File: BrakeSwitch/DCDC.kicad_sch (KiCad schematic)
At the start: 7 parts, among them U1 XL1509-5.0

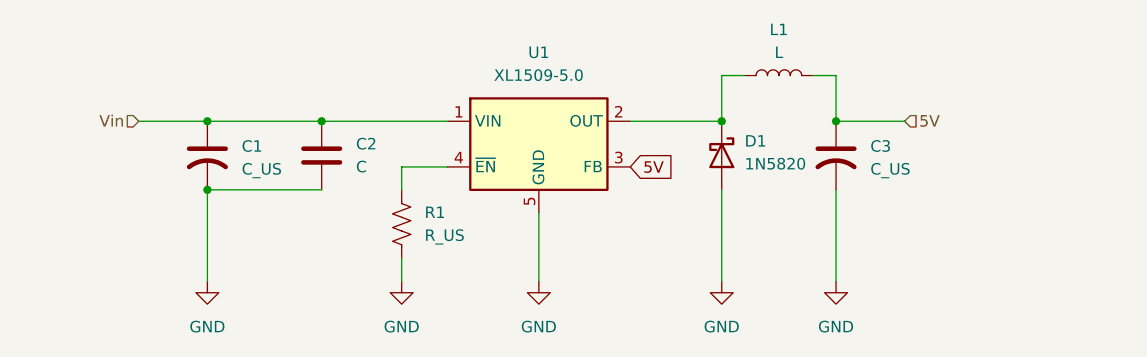
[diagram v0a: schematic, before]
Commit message: Assigned most footprints
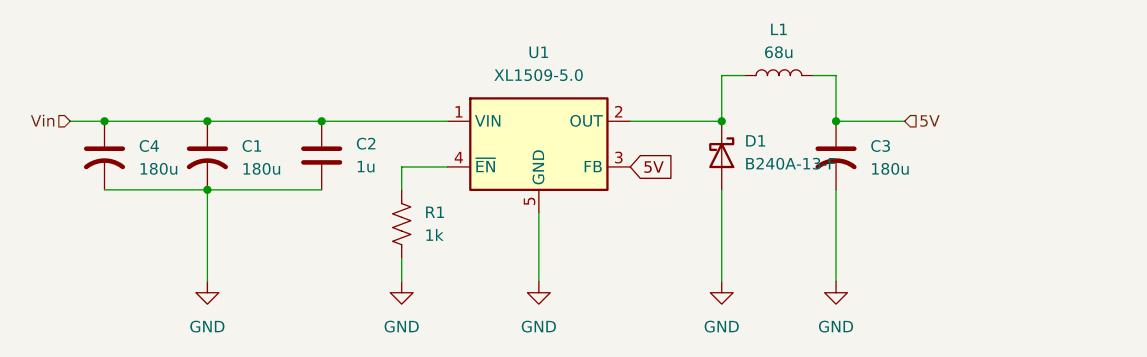
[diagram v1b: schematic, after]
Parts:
- added C4: 180u, Capacitor_SMD:CP_Elec_8x10.5, symbol Device:C_US
- C1, C3: value C_US -> 180u; footprint (none) -> Capacitor_SMD:CP_Elec_8x10.5
- C2: value C -> 1u; footprint (none) -> Capacitor_SMD:C_0603_1608Metric_Pad1.08x0.95mm_HandSolder
- D1: value 1N5820 -> B240A-13-F; footprint (none) -> Diode_SMD:D_SMA; DigiKey (none) -> https://www.digikey.com/en/products/detail/diodes-incorpora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
- L1: value L -> 68u; footprint (none) -> Inductor_SMD:L_12x12mm_H4.5mm; DigiKey (none) -> https://www.digikey.com/en/products/detail/sumida-america-i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
- R1: value R_US -> 1k; footprint (none) -> Resistor_SMD:R_0603_1608Metric
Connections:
- net GND: now also C4.2
- net Vin: now also C4.1
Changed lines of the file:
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@@
+	)
+	(junction
+		(at 20.32 26.67)
+		(diameter 0)
+		(color 0 0 0 0)
+	)
+	(junction
+		(at 31.75 34.29)
+		(diameter 0)
+		(color 0 0 0 0)
 	)
 	(junction
@@
 		(color 0 0 0 0)
 	)
-	(junction
-		(at 31.75 34.29)
-		(diameter 0)
-		(color 0 0 0 0)
-	)
 	(wire
 		(pts
@@
 	(wire
 		(pts
-			(xy 24.13 26.67) (xy 31.75 26.67)
+			(xy 31.75 26.67) (xy 44.45 26.67)
 		)
 		(stroke
@@
 	(wire
 		(pts
-			(xy 88.9 21.59) (xy 91.44 21.59)
+			(xy 16.51 26.67) (xy 20.32 26.67)
 		)
 		(stroke
@@
 	(wire
 		(pts
-			(xy 101.6 34.29) (xy 101.6 44.45)
+			(xy 88.9 21.59) (xy 91.44 21.59)
 		)
 		(stroke
@@
 	(wire
 		(pts
-			(xy 68.58 36.83) (xy 68.58 44.45)
+			(xy 20.32 26.67) (xy 31.75 26.67)
 		)
 		(stroke
@@
 	(wire
 		(pts
-			(xy 31.75 26.67) (xy 44.45 26.67)
+			(xy 101.6 34.29) (xy 101.6 44.45)
 		)
 		(stroke
@@
 	(wire
 		(pts
-			(xy 88.9 34.29) (xy 88.9 44.45)
+			(xy 68.58 36.83) (xy 68.58 44.45)
 		)
 		(stroke
@@
 	(wire
 		(pts
-			(xy 101.6 21.59) (xy 101.6 26.67)
+			(xy 88.9 34.29) (xy 88.9 44.45)
 		)
 		(stroke
@@
 	(wire
 		(pts
-			(xy 101.6 26.67) (xy 109.22 26.67)
+			(xy 101.6 21.59) (xy 101.6 26.67)
 		)
 		(stroke
@@
 	(wire
 		(pts
-			(xy 78.74 26.67) (xy 88.9 26.67)
+			(xy 101.6 26.67) (xy 109.22 26.67)
 		)
 		(stroke
@@
 	(wire
 		(pts
+			(xy 78.74 26.67) (xy 88.9 26.67)
+		)
+		(stroke
+			(width 0)
+			(type default)
+		)
+	)
+	(wire
+		(pts
 			(xy 53.34 34.29) (xy 53.34 31.75)
+		)
+		(stroke
+			(width 0)
+			(type default)
+		)
+	)
+	(wire
+		(pts
+			(xy 31.75 34.29) (xy 20.32 34.29)
 		)
 		(stroke
@@
 	(hierarchical_label "Vin"
 		(shape input)
-		(at 24.13 26.67 180)
+		(at 16.51 26.67 180)
 		(effects
 			(font
@@
 	(symbol
 		(lib_id "Device:C_US")
+		(at 20.32 30.48 0)
+		(unit 1)
+		(exclude_from_sim no)
+		(in_bom yes)
+		(on_board yes)
+		(dnp no)
+		(fields_autoplaced yes)
+		(property "Reference" "C4"
+			(at 24.13 29.4639 0)
+			(effects
+				(font
+					(size 1.27 1.27)
+				)
+				(justify left)
+			)
+		)
+		(property "Value" "180u"
+			(at 24.13 32.0039 0)
+			(effects
+				(font
+					(size 1.27 1.27)
+				)
+				(justify left)
+			)
+		)
+		(property "Footprint" "Capacitor_SMD:CP_Elec_8x10.5"
+			(at 20.32 30.48 0)
+			(effects
+				(font
+					(size 1.27 1.27)
+				)
+				(hide yes)
+			)
+		)
+		(property "Datasheet" ""
+			(at 20.32 30.48 0)
+			(effects
+				(font
+					(size 1.27 1.27)
+				)
+				(hide yes)
+			)
+		)
+		(property "Description" "capacitor, US symbol"
+			(at 20.32 30.48 0)
+			(effects
+				(font
+					(size 1.27 1.27)
+				)
+				(hide yes)
+			)
+		)
+		(pin "2"
+		)
+		(pin "1"
+		)
+		(instances
+			(project "BrakeSwitch"
+				(path "/fe3f2fb8-8742-4f31-813f-1dad9d418d71/293b1cf4-e9c5-4398-be38-45432f0835da"
+					(reference "C4")
+					(unit 1)
+				)
+			)
+		)
+	)
+	(symbol
+		(lib_id "Device:C_US")
 		(at 101.6 30.48 0)
 		(unit 1)
@@
 			)
 		)
-		(property "Value" "C_US"
+		(property "Value" "180u"
 			(at 105.41 32.0039 0)
 			(effects
@@
 			)
 		)
-		(property "Footprint" ""
+		(property "Footprint" "Capacitor_SMD:CP_Elec_8x10.5"
 			(at 101.6 30.48 0)
 			(effects
@@
 			)
 		)
-		(property "Value" "R_US"
+		(property "Value" "1k"
 			(at 55.88 39.3699 0)
 			(effects
@@
 			)
 		)
-		(property "Footprint" ""
+		(property "Footprint" "Resistor_SMD:R_0603_1608Metric"
 			(at 54.356 38.354 90)
 			(effects
@@
 				(path "/fe3f2fb8-8742-4f31-813f-1dad9d418d71/293b1cf4-e9c5-4398-be38-45432f0835da"
 					(reference "R1")
+					(unit 1)
+				)
+			)
+		)
+	)
+	(symbol
+		(lib_id "Device:C_US")
+		(at 31.75 30.48 0)
+		(unit 1)
+		(exclude_from_sim no)
+		(in_bom yes)
+		(on_board yes)
+		(dnp no)
+		(fields_autoplaced yes)
+		(property "Reference" "C1"
+			(at 35.56 29.4639 0)
+			(effects
+				(font
+					(size 1.27 1.27)
+				)
+				(justify left)
+			)
+		)
+		(property "Value" "180u"
+			(at 35.56 32.0039 0)
+			(effects
+				(font
+					(size 1.27 1.27)
+				)
+				(justify left)
+			)
+		)
+		(property "Footprint" "Capacitor_SMD:CP_Elec_8x10.5"
+			(at 31.75 30.48 0)
+			(effects
+				(font
+					(size 1.27 1.27)
+				)
+				(hide yes)
+			)
+		)
+		(property "Datasheet" ""
+			(at 31.75 30.48 0)
+			(effects
+				(font
+					(size 1.27 1.27)
+				)
+				(hide yes)
+			)
+		)
+		(property "Description" "capacitor, US symbol"
+			(at 31.75 30.48 0)
+			(effects
+				(font
+					(size 1.27 1.27)
+				)
+				(hide yes)
+			)
+		)
+		(pin "2"
+		)
+		(pin "1"
+		)
+		(instances
+			(project "BrakeSwitch"
+				(path "/fe3f2fb8-8742-4f31-813f-1dad9d418d71/293b1cf4-e9c5-4398-be38-45432f0835da"
+					(reference "C1")
 					(unit 1)
 				)
@@
 			)
 		)
-		(property "Value" "C"
+		(property "Value" "1u"
 			(at 48.26 31.7499 0)
 			(effects
@@
 			)
 		)
-		(property "Footprint" ""
+		(property "Footprint" "Capacitor_SMD:C_0603_1608Metric_Pad1.08x0.95mm_HandSolder"
 			(at 45.4152 34.29 0)
 			(effects
@@
 			)
 		)
-		(property "Value" "1N5820"
+		(property "Value" "B240A-13-F"
 			(at 91.44 31.4324 90)
 			(effects
@@
 			)
 		)
-		(property "Footprint" ""
+		(property "Footprint" "Diode_SMD:D_SMA"
 			(at 88.9 30.48 0)
 			(effects
@@
 			)
 		)
-		(property "Datasheet" "~"
+		(property "Datasheet" "https://www.diodes.com/assets/Datasheets/B220_A-B260_A.pdf"
 			(at 88.9 30.48 0)
 			(effects
@@
 		(property "Description" "Schottky diode"
 			(at 88.9 30.48 0)
+			(effects
+				(font
+					(size 1.27 1.27)
+				)
+				(hide yes)
+			)
+		)
+		(property "DigiKey" "https://www.digikey.com/en/products/detail/diodes-incorporated/B240A-13-F/717691"
+			(at 88.9 30.48 90)
 			(effects
 				(font
@@
 			)
 		)
-		(property "Value" "L"
+		(property "Value" "68u"
 			(at 95.25 19.05 90)
 			(effects
@@
 			)
 		)
-		(property "Footprint" ""
+		(property "Footprint" "Inductor_SMD:L_12x12mm_H4.5mm"
 			(at 95.25 21.59 0)
 			(effects
@@
 		(property "Description" "Inductor"
 			(at 95.25 21.59 0)
+			(effects
+				(font
+					(size 1.27 1.27)
+				)
+				(hide yes)
+			)
+		)
+		(property "DigiKey" "https://www.digikey.com/en/products/detail/sumida-america-inc/CDRH124NP-680MC/3947049"
+			(at 95.25 21.59 90)
 			(effects
 				(font
@@
 					(unit 1)
 				)
-			)
-		)
-	)
-	(symbol
-		(lib_id "Device:C_US")
-		(at 31.75 30.48 0)
-		(unit 1)
-		(exclude_from_sim no)
-		(in_bom yes)
-		(on_board yes)
-		(dnp no)
-		(fields_autoplaced yes)
-		(property "Reference" "C1"
-			(at 35.56 29.4639 0)
-			(effects
-				(font
-					(size 1.27 1.27)
-				)
-				(justify left)
-			)
-		)
-		(property "Value" "C_US"
-			(at 35.56 32.0039 0)
-			(effects
-				(font
-					(size 1.27 1.27)
-				)
-				(justify left)
-			)
-		)
-		(property "Footprint" ""
-			(at 31.75 30.48 0)
-			(effects
-				(font
-					(size 1.27 1.27)
-				)
-				(hide yes)
-			)
-		)
-		(property "Datasheet" ""
-			(at 31.75 30.48 0)
-			(effects
-				(font
-					(size 1.27 1.27)
-				)
-				(hide yes)
-			)
-		)
-		(property "Description" "capacitor, US symbol"
-			(at 31.75 30.48 0)
-			(effects
-				(font
-					(size 1.27 1.27)
-				)
-				(hide yes)
-			)
-		)
-		(pin "2"
-		)
-		(pin "1"
-		)
-		(instances
-			(project "BrakeSwitch"
-				(path "/fe3f2fb8-8742-4f31-813f-1dad9d418d71/293b1cf4-e9c5-4398-be38-45432f0835da"
-					(reference "C1")
-					(unit 1)
-				)

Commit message: Basic layout done
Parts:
- added C5, C6: 1u, Capacitor_SMD:C_0603_1608Metric_Pad1.08x0.95mm_HandSolder, symbol Device:C
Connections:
- net 5V: now also C5.1, C6.1
- net GND: now also C5.2, C6.2
